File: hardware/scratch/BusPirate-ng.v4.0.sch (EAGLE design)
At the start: 142 parts, among them CON1 CON-USB-F-MICRO-B, IC1 IC_UC_STM32F103RBTXX-LQFP64, IC10 74LVC1G07DBV, IC11 IC_BUFF_SN74LVC1T45DBV, IC12 74LVC1G07DBV, IC13 IC_BUFF_SN74LVC1T45DBV, IC14 74LVC1G07DBV, IC15 IC_BUFF_SN74LVC1T45DBV, IC16 74LVC1G07DBV, IC17 IC_BUFF_SN74LVC1T45DBV, IC2 IC_MEM_23LC1024, IC3 IC_MEM_23LC1024, IC4 IC_74AC573, IC5 IC_BL1551, IC6 IC_BL1551, IC7 74HCT4066PW, IC8 74LVC1G07DBV, IC9 IC_BUFF_SN74LVC1T45DBV, J1 CON_HEADER_1X04, J2 CON_HEADER_1X03-PTH, J3 CON_HEADER_2X02-PTH, J4 CON_HEADER_1X10-RIGHT_ANGLED_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, U1 IC_FPGA_ICE40HX4K, U2 IC_UC_STM32F103ZX, U3 IC_MEM_AT45DB041D

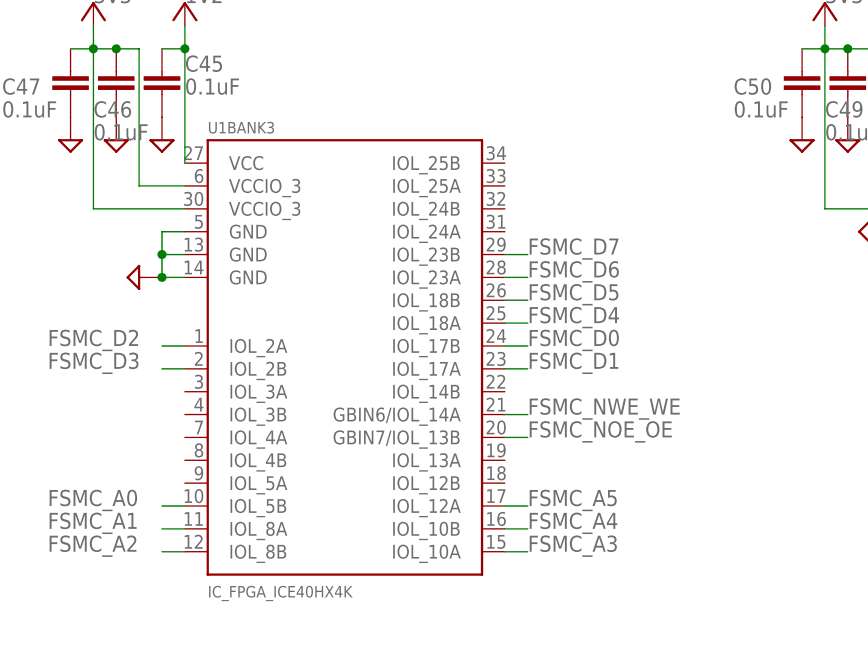
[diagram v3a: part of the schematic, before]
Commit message: removed connection FSMC_NOE_OE and FSMC_NEW_WE wired FSMC_D8 - FSMC_D15 to FPGA
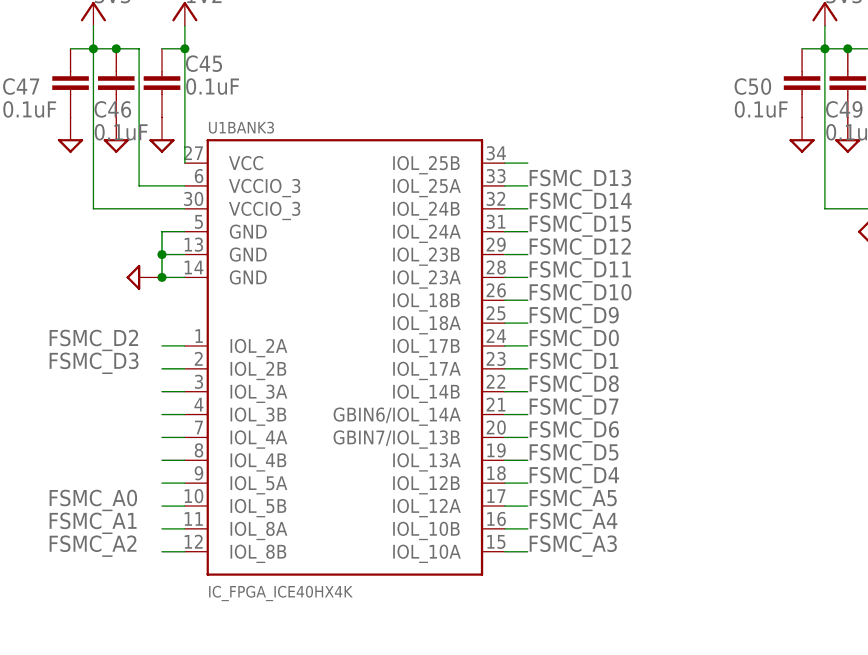
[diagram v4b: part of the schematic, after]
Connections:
- new net N$11: U1BANK3.IOL_3A
- new net N$15: U1BANK3.IOL_3B
- new net N$17: U1BANK3.IOL_25B
- new net N$19: U1BANK3.IOL_4A
- new net N$21: U1BANK3.IOL_4B
- new net N$22: U1BANK3.IOL_5A
- net FSMC_D10: now also U1BANK3.IOL_18B
- net FSMC_D11: now also U1BANK3.IOL_23A
- net FSMC_D12: now also U1BANK3.IOL_23B
- net FSMC_D13: now also U1BANK3.IOL_25A
- net FSMC_D14: now also U1BANK3.IOL_24B
- net FSMC_D15: now also U1BANK3.IOL_24A
- net FSMC_D4: now also U1BANK3.IOL_12B; no longer U1BANK3.IOL_18A
- net FSMC_D5: now also U1BANK3.IOL_13A; no longer U1BANK3.IOL_18B
- net FSMC_D6: now also U1BANK3.GBIN7/IOL_13B; no longer U1BANK3.IOL_23A
- net FSMC_D7: now also U1BANK3.GBIN6/IOL_14A; no longer U1BANK3.IOL_23B
- net FSMC_D8: now also U1BANK3.IOL_14B
- net FSMC_D9: now also U1BANK3.IOL_18A
- net FSMC_NOE_OE: no longer U1BANK3.GBIN7/IOL_13B
- net FSMC_NWE_WE: no longer U1BANK3.GBIN6/IOL_14A
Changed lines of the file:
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@@
 <label x="-241.3" y="416.56" size="1.778" layer="95"/>
+</segment>
+</net>
+<net name="FSMC_NWE_WE" class="0">
+<segment>
+<pinref part="U2" gate="U" pin="PD5/FT/FSMC_NWE/USART2_TX('1')"/>
+<wire x1="-215.9" y1="414.02" x2="-228.6" y2="414.02" width="0.1524" layer="91"/>
+<label x="-241.3" y="414.02" size="1.778" layer="95"/>
+</segment>
+</net>
+<net name="FSMC_D0" class="0">
+<segment>
+<pinref part="U2" gate="U" pin="PD14/FT/FSMC_D0/TIM4_CH3('1')"/>
+<wire x1="-215.9" y1="391.16" x2="-228.6" y2="391.16" width="0.1524" layer="91"/>
+<label x="-238.76" y="391.16" size="1.778" layer="95"/>
+</segment>
+<segment>
+<pinref part="U1" gate="BANK3" pin="IOL_17B"/>
+<wire x1="-2.54" y1="370.84" x2="0" y2="370.84" width="0.1524" layer="91"/>
+<label x="0" y="370.84" size="1.778" layer="95"/>
+</segment>
+</net>
+<net name="FSMC_D1" class="0">
+<segment>
+<pinref part="U2" gate="U" pin="PD15/FT/FSMC_D1/TIM4_CH4('1')"/>
+<wire x1="-215.9" y1="388.62" x2="-228.6" y2="388.62" width="0.1524" layer="91"/>
+<label x="-238.76" y="388.62" size="1.778" layer="95"/>
+</segment>
+<segment>
+<pinref part="U1" gate="BANK3" pin="IOL_17A"/>
+<wire x1="-2.54" y1="368.3" x2="0" y2="368.3" width="0.1524" layer="91"/>
+<label x="0" y="368.3" size="1.778" layer="95"/>
+</segment>
+</net>
+<net name="FSMC_D4" class="0">
+<segment>
+<pinref part="U2" gate="U" pin="PE7/FT/FSMC_D4/TIM1_ETR('11')"/>
+<wire x1="-215.9" y1="365.76" x2="-228.6" y2="365.76" width="0.1524" layer="91"/>
+<label x="-238.76" y="365.76" size="1.778" layer="95"/>
+</segment>
+<segment>
+<pinref part="U1" gate="BANK3" pin="IOL_12B"/>
+<wire x1="-2.54" y1="355.6" x2="0" y2="355.6" width="0.1524" layer="91"/>
+<label x="0" y="355.6" size="1.778" layer="95"/>
+</segment>
+</net>
+<net name="FSMC_D5" class="0">
+<segment>
+<pinref part="U2" gate="U" pin="PE8/FT/FSMC_D5/TIM1_CH1N('11')"/>
+<wire x1="-215.9" y1="363.22" x2="-228.6" y2="363.22" width="0.1524" layer="91"/>
+<label x="-238.76" y="363.22" size="1.778" layer="95"/>
+</segment>
+<segment>
+<pinref part="U1" gate="BANK3" pin="IOL_13A"/>
+<wire x1="-2.54" y1="358.14" x2="0" y2="358.14" width="0.1524" layer="91"/>
+<label x="0" y="358.14" size="1.778" layer="95"/>
+</segment>
+</net>
+<net name="FSMC_D6" class="0">
+<segment>
+<pinref part="U2" gate="U" pin="PE9/FT/FSMC_D6/TIM1_CH1('11')"/>
+<wire x1="-215.9" y1="360.68" x2="-228.6" y2="360.68" width="0.1524" layer="91"/>
+<label x="-238.76" y="360.68" size="1.778" layer="95"/>
 </segment>
 <segment>
@@
 </segment>
 </net>
-<net name="FSMC_NWE_WE" class="0">
-<segment>
-<pinref part="U2" gate="U" pin="PD5/FT/FSMC_NWE/USART2_TX('1')"/>
-<wire x1="-215.9" y1="414.02" x2="-228.6" y2="414.02" width="0.1524" layer="91"/>
-<label x="-241.3" y="414.02" size="1.778" layer="95"/>
+<net name="FSMC_D7" class="0">
+<segment>
+<pinref part="U2" gate="U" pin="PE10/FT/FSMC_D7/TIM1_CH2N('11')"/>
+<wire x1="-215.9" y1="358.14" x2="-228.6" y2="358.14" width="0.1524" layer="91"/>
+<label x="-238.76" y="358.14" size="1.778" layer="95"/>
 </segment>
 <segment>
@@
 <wire x1="-2.54" y1="363.22" x2="0" y2="363.22" width="0.1524" layer="91"/>
 <label x="0" y="363.22" size="1.778" layer="95"/>
-</segment>
-</net>
-<net name="FSMC_D0" class="0">
-<segment>
-<pinref part="U2" gate="U" pin="PD14/FT/FSMC_D0/TIM4_CH3('1')"/>
-<wire x1="-215.9" y1="391.16" x2="-228.6" y2="391.16" width="0.1524" layer="91"/>
-<label x="-238.76" y="391.16" size="1.778" layer="95"/>
-</segment>
-<segment>
-<pinref part="U1" gate="BANK3" pin="IOL_17B"/>
-<wire x1="-2.54" y1="370.84" x2="0" y2="370.84" width="0.1524" layer="91"/>
-<label x="0" y="370.84" size="1.778" layer="95"/>
-</segment>
-</net>
-<net name="FSMC_D1" class="0">
-<segment>
-<pinref part="U2" gate="U" pin="PD15/FT/FSMC_D1/TIM4_CH4('1')"/>
-<wire x1="-215.9" y1="388.62" x2="-228.6" y2="388.62" width="0.1524" layer="91"/>
-<label x="-238.76" y="388.62" size="1.778" layer="95"/>
-</segment>
-<segment>
-<pinref part="U1" gate="BANK3" pin="IOL_17A"/>
-<wire x1="-2.54" y1="368.3" x2="0" y2="368.3" width="0.1524" layer="91"/>
-<label x="0" y="368.3" size="1.778" layer="95"/>
-</segment>
-</net>
-<net name="FSMC_D4" class="0">
-<segment>
-<pinref part="U2" gate="U" pin="PE7/FT/FSMC_D4/TIM1_ETR('11')"/>
-<wire x1="-215.9" y1="365.76" x2="-228.6" y2="365.76" width="0.1524" layer="91"/>
-<label x="-238.76" y="365.76" size="1.778" layer="95"/>
-</segment>
-<segment>
-<pinref part="U1" gate="BANK3" pin="IOL_18A"/>
-<wire x1="-2.54" y1="373.38" x2="0" y2="373.38" width="0.1524" layer="91"/>
-<label x="0" y="373.38" size="1.778" layer="95"/>
-</segment>
-</net>
-<net name="FSMC_D5" class="0">
-<segment>
-<pinref part="U2" gate="U" pin="PE8/FT/FSMC_D5/TIM1_CH1N('11')"/>
-<wire x1="-215.9" y1="363.22" x2="-228.6" y2="363.22" width="0.1524" layer="91"/>
-<label x="-238.76" y="363.22" size="1.778" layer="95"/>
-</segment>
-<segment>
-<pinref part="U1" gate="BANK3" pin="IOL_18B"/>
-<wire x1="-2.54" y1="375.92" x2="0" y2="375.92" width="0.1524" layer="91"/>
-<label x="0" y="375.92" size="1.778" layer="95"/>
-</segment>
-</net>
-<net name="FSMC_D6" class="0">
-<segment>
-<pinref part="U2" gate="U" pin="PE9/FT/FSMC_D6/TIM1_CH1('11')"/>
-<wire x1="-215.9" y1="360.68" x2="-228.6" y2="360.68" width="0.1524" layer="91"/>
-<label x="-238.76" y="360.68" size="1.778" layer="95"/>
-</segment>
-<segment>
-<pinref part="U1" gate="BANK3" pin="IOL_23A"/>
-<wire x1="-2.54" y1="378.46" x2="0" y2="378.46" width="0.1524" layer="91"/>
-<label x="0" y="378.46" size="1.778" layer="95"/>
-</segment>
-</net>
-<net name="FSMC_D7" class="0">
-<segment>
-<pinref part="U2" gate="U" pin="PE10/FT/FSMC_D7/TIM1_CH2N('11')"/>
-<wire x1="-215.9" y1="358.14" x2="-228.6" y2="358.14" width="0.1524" layer="91"/>
-<label x="-238.76" y="358.14" size="1.778" layer="95"/>
-</segment>
-<segment>
-<pinref part="U1" gate="BANK3" pin="IOL_23B"/>
-<wire x1="-2.54" y1="381" x2="0" y2="381" width="0.1524" layer="91"/>
-<label x="0" y="381" size="1.778" layer="95"/>
 </segment>
 </net>
@@
 <label x="-238.76" y="355.6" size="1.778" layer="95"/>
 </segment>
+<segment>
+<pinref part="U1" gate="BANK3" pin="IOL_14B"/>
+<wire x1="-2.54" y1="365.76" x2="0" y2="365.76" width="0.1524" layer="91"/>
+<label x="0" y="365.76" size="1.778" layer="95"/>
+</segment>
 </net>
 <net name="FSMC_D9" class="0">
@@
 <label x="-238.76" y="353.06" size="1.778" layer="95"/>
 </segment>
+<segment>
+<pinref part="U1" gate="BANK3" pin="IOL_18A"/>
+<wire x1="-2.54" y1="373.38" x2="0" y2="373.38" width="0.1524" layer="91"/>
+<label x="0" y="373.38" size="1.778" layer="95"/>
+</segment>
 </net>
 <net name="FSMC_D10" class="0">
@@
 <label x="-238.76" y="350.52" size="1.778" layer="95"/>
 </segment>
+<segment>
+<pinref part="U1" gate="BANK3" pin="IOL_18B"/>
+<wire x1="-2.54" y1="375.92" x2="0" y2="375.92" width="0.1524" layer="91"/>
+<label x="0" y="375.92" size="1.778" layer="95"/>
+</segment>
 </net>
 <net name="FSMC_D11" class="0">
@@
 <label x="-238.76" y="347.98" size="1.778" layer="95"/>
 </segment>
+<segment>
+<pinref part="U1" gate="BANK3" pin="IOL_23A"/>
+<wire x1="-2.54" y1="378.46" x2="0" y2="378.46" width="0.1524" layer="91"/>
+<label x="0" y="378.46" size="1.778" layer="95"/>
+</segment>
 </net>
 <net name="FSMC_D12" class="0">
@@
 <label x="-238.76" y="345.44" size="1.778" layer="95"/>
 </segment>
+<segment>
+<pinref part="U1" gate="BANK3" pin="IOL_23B"/>
+<wire x1="-2.54" y1="381" x2="0" y2="381" width="0.1524" layer="91"/>
+<label x="0" y="381" size="1.778" layer="95"/>
+</segment>
 </net>
 <net name="FSMC_D13" class="0">
@@
 <label x="-241.3" y="406.4" size="1.778" layer="95"/>
 </segment>
+<segment>
+<pinref part="U1" gate="BANK3" pin="IOL_25A"/>
+<wire x1="-2.54" y1="388.62" x2="0" y2="388.62" width="0.1524" layer="91"/>
+<label x="0" y="388.62" size="1.778" layer="95"/>
+</segment>
 </net>
 <net name="FSMC_D14" class="0">
@@
 <label x="-241.3" y="403.86" size="1.778" layer="95"/>
 </segment>
+<segment>
+<pinref part="U1" gate="BANK3" pin="IOL_24B"/>
+<wire x1="-2.54" y1="386.08" x2="0" y2="386.08" width="0.1524" layer="91"/>
+<label x="0" y="386.08" size="1.778" layer="95"/>
+</segment>
 </net>
 <net name="FSMC_D15" class="0">
@@
 <label x="-241.3" y="401.32" size="1.778" layer="95"/>
 </segment>
-</net>
+<segment>
+<pinref part="U1" gate="BANK3" pin="IOL_24A"/>
+<wire x1="-2.54" y1="383.54" x2="0" y2="383.54" width="0.1524" layer="91"/>
+<label x="0" y="383.54" size="1.778" layer="95"/>
+</segment>
+</net>
+<net name="N$17" class="0">
+<segment>
+<pinref part="U1" gate="BANK3" pin="IOL_25B"/>
+<wire x1="-2.54" y1="391.16" x2="0" y2="391.16" width="0.1524" layer="91"/>
+</segment>
+</net>
+<net name="N$11" class="0">
+<segment>
+<pinref part="U1" gate="BANK3" pin="IOL_3A"/>
+<wire x1="-38.1" y1="365.76" x2="-40.64" y2="365.76" width="0.1524" layer="91"/>
+</segment>
+</net>
+<net name="N$15" class="0">
+<segment>
+<pinref part="U1" gate="BANK3" pin="IOL_3B"/>
+<wire x1="-38.1" y1="363.22" x2="-40.64" y2="363.22" width="0.1524" layer="91"/>
+</segment>
+</net>
+<net name="N$19" class="0">
+<segment>
+<pinref part="U1" gate="BANK3" pin="IOL_4A"/>
+<wire x1="-38.1" y1="360.68" x2="-40.64" y2="360.68" width="0.1524" layer="91"/>
+</segment>
+</net>
+<net name="N$21" class="0">
+<segment>
+<pinref part="U1" gate="BANK3" pin="IOL_4B"/>
+<wire x1="-38.1" y1="358.14" x2="-40.64" y2="358.14" width="0.1524" layer="91"/>
+</segment>
+</net>
+<net name="N$22" class="0">
+<segment>
+<pinref part="U1" gate="BANK3" pin="IOL_5A"/>
+<wire x1="-38.1" y1="355.6" x2="-40.64" y2="355.6" width="0.1524" layer="91"/>
+</segment>
+</net>

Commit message: wired: -IO headers -CRESET -CDONE -MCU_MCO (Master Clock Out) to FPGA -FPGA to IO buffers -VCCPLL with 0.1uF cap and GNDPLL -2 interrupts from FPGA but not yet connected
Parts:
- added C55: 0.1uF, rcl:C-EUC0603
- added J5: CON_HEADER_1X10-RIGHT_ANGLED_PTH_SHROUDED, dp_devices.v6:CON_HEADER_1X10-RIGHT_ANGLED_PTH_SHROUDED
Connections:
- removed net N$11: U1BANK3.IOL_3A
- removed net N$12: R38.1, U1BANK2.CRESET_B
- removed net N$14: R39.1, U1BANK2.CDONE
- new net FPGA_CDONE: R39.1, U1BANK2.CDONE, U2U.I2C2_SDA/USART3_RX('00')/TIM2_CH4('10'OR'11')/FT/PB11
- new net FPGA_CRESET: R38.1, U1BANK2.CRESET_B, U2U.I2C2_SCL/USART3_TX('00')/TIM2_CH3('10'OR'11')/FT/PB10
- new net MCU_INT0: U1BANK2.GBIN4/IOB_82
- new net MCU_INT1: U1BANK2.GBIN5/IOB_81
- new net MCU_MCO: U1BANK3.GBIN7/IOL_13B, U2U.PA8/FT/USART1_CK/TIM1_CH1('00'OR'01')/MCO
- new net N$10: U2U.PG0/FT/FSMC_A10
- new net N$23: U1BANK0.IOT_168
- new net N$24: U1BANK0.GBIN0/IOT_198
- new net N$25: U1BANK0.GBIN1/IOT_197
- net 1V2: now also C55.2, U1BANK2.VCCPLL0
- net BPIO_AUX: now also J5.6
- net BPIO_CLOCK: now also J5.9
- net BPIO_CS: now also J5.7
- net BPIO_MISO: now also J5.8
- net BPIO_MOSI: now also J5.10
- net BUFDIR_AUX: now also U1BANK1.IOR_144
- net BUFDIR_CLOCK: now also U1BANK1.IOR_164
- net BUFDIR_CS: now also U1BANK1.IOR_139
- net BUFDIR_MISO: now also U1BANK1.IOR_152
- net BUFDIR_MOSI: now also U1BANK1.IOR_167
- net BUFIO_AUX: now also U1BANK1.GBIN2/IOR_141
- net BUFIO_CLOCK: now also U1BANK1.IOR_161
- net BUFIO_CS: now also U1BANK1.IOR_138
- net BUFIO_MISO: now also U1BANK1.IOR_148
- net BUFIO_MOSI: now also U1BANK1.IOR_166
- net BUFOD_AUX: now also U1BANK1.GBIN3/IOR_140
- net BUFOD_CLOCK: now also U1BANK1.IOR_160
- net BUFOD_CS: now also U1BANK1.IOR_137
- net BUFOD_MISO: now also U1BANK1.IOR_147
- net BUFOD_MOSI: now also U1BANK1.IOR_165
- net FSMC_A0: now also U1BANK3.IOL_3A; no longer U1BANK3.IOL_5B
- net FSMC_A1: now also U1BANK3.IOL_3B; no longer U1BANK3.IOL_8A
- net FSMC_A2: now also U1BANK3.IOL_4A; no longer U1BANK3.IOL_8B
- net FSMC_A3: now also U1BANK3.IOL_4B; no longer U1BANK3.IOL_10A
- net FSMC_A4: now also U1BANK3.IOL_5A; no longer U1BANK3.IOL_10B
- net FSMC_A5: now also U1BANK3.IOL_5B; no longer U1BANK3.IOL_12A
- net FSMC_D4: now also U1BANK3.IOL_10A; no longer U1BANK3.IOL_12B
- net FSMC_D5: now also U1BANK3.IOL_10B; no longer U1BANK3.IOL_13A
- net FSMC_D6: now also U1BANK3.IOL_12A; no longer U1BANK3.GBIN7/IOL_13B
- net FSMC_D7: now also U1BANK3.IOL_12B; no longer U1BANK3.GBIN6/IOL_14A
- net FSMC_D8: now also U1BANK3.IOL_13A; no longer U1BANK3.IOL_14B
- net GND: now also C55.1, J5.1, U1BANK0.GNDPLL1, U1BANK2.GNDPLL0
- net IO_ADC/DAC: now also J5.5
- net N$15: now also U1BANK3.IOL_8A; no longer U1BANK3.IOL_3B
- net N$19: now also U1BANK3.IOL_8B; no longer U1BANK3.IOL_4A
- net N$21: now also U1BANK3.GBIN6/IOL_14A; no longer U1BANK3.IOL_4B
- net N$22: now also U1BANK3.IOL_14B; no longer U1BANK3.IOL_5A
- net SWV33: now also J5.3
- net SWV50: now also J5.2
- net VEXTERN: now also J5.4
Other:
- note removed: "gndpll nc?!?"

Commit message: wired Logic analyzer circuit to FPGA
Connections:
- net IO_OE: now also U1BANK0.IOT_206
- net LA_AUX0: now also U1BANK0.IOT_215
- net LA_CLK: now also U1BANK0.IOT_221
- net LA_CS: now also U1BANK0.IOT_219
- net LA_HOLD: now also U1BANK0.IOT_212
- net LA_MISO: now also U1BANK0.IOT_222
- net LA_MOSI: now also U1BANK0.IOT_220
- net LA_SWV33: now also U1BANK0.IOT_214
- net LA_SWV50: now also U1BANK0.IOT_213
- net SRAM_CLK: now also U1BANK0.IOT_217
- net SRAM_CS: now also U1BANK0.IOT_216
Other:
- moved on the sheet: C14, C15, C17, IC2, IC3, IC4

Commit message: routing started, switch to bigger DP8556 PCB
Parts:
- removed C1, C3: 22pF, rcl:C-EUC0603
- removed C10, C2, C20, C4, C5, C7, C8, C9: 0.1uF, rcl:C-EUC0603
- removed C6: 1uF, rcl:CPOL-EUSMCA
- removed IC1: IC_UC_STM32F103RBTXX-LQFP64, dp_devices:IC_UC_STM32F103RBTXX-LQFP64
- removed PCB1: PCB_DP_RECTANGLE-80X49, dp_devices:PCB_DP_RECTANGLE-80X49
- removed R1: 10K, dp_devices:RESISTOR-0603
- removed XTAL1: 8Mhz, dp_devices:OSC-XTAL-12M
- added PCB2: PCB_DP_RECTANGLE-85X56, dp_blank_pcb:PCB_DP_RECTANGLE-85X56
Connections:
- removed net N$16: C3.2, IC1.PD0/5V/OSC_IN, XTAL1.2
- removed net N$20: C1.2, IC1.PD1/5V/OSC_OUT, XTAL1.1
- net 3V3: no longer C10.2, C20.2, C4.2, C5.2, C6.+, C7.2, C8.2, C9.2, IC1.VBAT, IC1.VDDA, IC1.VDD_1, IC1.VDD_2, IC1.VDD_3, IC1.VDD_4
- net ADC1: no longer IC1.TIM3_CH4/ADC9/PB1
- net ADC2: no longer IC1.ADC13/PC3
- net ADC3: no longer IC1.ADC11/PC1
- net ADC4: no longer IC1.ADC12/PC2
- net ADC5: no longer IC1.ADC10/PC0
- net ADC6: no longer IC1.ADC14/PC4
- net AUX0: no longer IC1.PD2/5V/TIM3_ETR, IC1.TIM3_CH3/ADC8/PB0
- net BOOT0: no longer IC1.BOOT0
- net BOOT1: no longer IC1.BOOT1/5V/PB2
- net CLOCK: no longer IC1.I2C1_SCL/TIM4_CH1/5V/PB6, IC1.SPI2_SCK/USART3_CTS/TIM1_CH1N/5V/PB13
- net CS: no longer IC1.SPI2_NSS/I2C2_SMBAI/USART3_CK/TIM1_BKIN/5V/PB12
- net GND: no longer C1.1, C10.1, C2.1, C20.1, C3.1, C4.1, C5.1, C6.-, C7.1, C8.1, C9.1, IC1.VSSA, IC1.VSS_1, IC1.VSS_2, IC1.VSS_3, IC1.VSS_4, R1.2
- net IO_OE: no longer IC1.5V/PC7
- net LA_AUX0: no longer IC1.PA4/ADC4/USART2_CK/SPI1_NSS
- net LA_CLK: no longer IC1.PA1/ADC1/USART2_RTS/TIM2_CH2
- net LA_CS: no longer IC1.PA3/ADC3/USART2_RX/TIM2_CH4
- net LA_HOLD: no longer IC1.PA7/ADC7/SPI1_MOSI/TIM3_CH2
- net LA_MISO: no longer IC1.PA2/ADC2/USART2_TX/TIM2_CH4
- net LA_MOSI: no longer IC1.PA0/ADC0/USART2_CTS/TIM2_CH1_ETR/WKUP
- net LA_SWV33: no longer IC1.PA5/ADC5/SPI1_SCK
- net LA_SWV50: no longer IC1.PA6/ADC6/SPI1_MISO/TIM3_CH1
- net LD1: no longer IC1.5V/PC8
- net MISO: no longer IC1.I2C2_SDA/USART3_RX/5V/PB11, IC1.SPI2_MISO/USART3_RTS/TIM1_CH2N/5V/PB14
- net MOSI: no longer IC1.I2C1_SDA/TIM4_CH2/5V/PB7, IC1.I2C2_SCL/USART3_TX/5V/PB10, IC1.SPI2_MOSI/TIM1_CH3N/5V/PB15
- net MS0: no longer IC1.TIM4_CH3/5V/PB8
- net RST: no longer C2.2, IC1.NRST
- net SRAM_CLK: no longer IC1.PA8/5V/USART1_CK/TIM1_CH1/MCO
- net SRAM_CS: no longer IC1.JTDO/5V/PB3
- net SWCLK: no longer IC1.PA14/5V/JTCK/SWCLK
- net SWDIO: no longer IC1.PA13/5V/JTMS/SWDIO
- net UART_RX: no longer IC1.PA10/5V/USART1_RX/TIM1_CH3
- net UART_TX: no longer IC1.PA9/5V/USART1_TX/TIM1_CH2
- net USBLED: no longer IC1.5V/PC9
- net USB_D+: no longer IC1.PA12/5V/USART1_RTS/TIM1_ETR/CAN_TX/USB_D+
- net USB_D-: no longer IC1.PA11/5V/USART1_CTS/TIM1_CH4/CAN_RX/USB_D-
- net USB_DET: no longer IC1.PA15/5V/JTDI
- net V33PU: no longer IC1.I2C1_SMBAI/PB5
- net V50PU: no longer IC1.JNTRST/5V/PB4
- net VEXTPU: no longer IC1.5V/PC6
- net VREGEN: no longer IC1.TIM4_CH4/5V/PB9, R1.1
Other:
- note removed: "STM32F103"
- note removed: "wire SRAM_CLK to FPGA global pin clock"
- moved on the sheet: C36, C37, C51, C52, C53, C54, R40, U2, XTAL2

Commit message: individualy wired SRAM to FPGA and LATCH to FPGA, continue routing
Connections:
- removed net LA_AUX0: IC3IC.SI/SIO0, IC4IC.4Q, U1BANK0.IOT_215
- removed net LA_CLK: IC2IC.SO/SIO1, IC4IC.7Q, U1BANK0.IOT_221
- removed net LA_CS: IC2IC.!HOLD/SIO3, IC4IC.5Q, U1BANK0.IOT_219
- removed net LA_HOLD: IC3IC.!HOLD/SIO3, U1BANK0.IOT_212
- removed net LA_MISO: IC2IC.SI/SIO0, IC4IC.6Q, U1BANK0.IOT_222
- removed net LA_MOSI: IC2IC.SIO2, IC4IC.8Q, U1BANK0.IOT_220
- removed net LA_SWV33: IC3IC.SO/SIO1, IC4IC.3Q, U1BANK0.IOT_214
- removed net LA_SWV50: IC3IC.SIO2, IC4IC.2Q, U1BANK0.IOT_213
- new net LA_LAT_AUX0: IC4IC.4Q, U1BANK0.IOT_170
- new net LA_LAT_CLK: IC4IC.7Q, U1BANK0.IOT_173
- new net LA_LAT_CS: IC4IC.5Q, U1BANK0.IOT_171
- new net LA_LAT_MISO: IC4IC.6Q, U1BANK0.IOT_172
- new net LA_LAT_MOSI: IC4IC.8Q, U1BANK0.IOT_174
- new net LA_LAT_SWV33: IC4IC.3Q, U1BANK0.IOT_169
- new net LA_LAT_SWV50: IC4IC.2Q, U1BANK0.IOT_168
- new net LA_MEM_AUX0: IC3IC.SI/SIO0, U1BANK0.IOT_212
- new net LA_MEM_CLK: IC2IC.SO/SIO1, U1BANK0.IOT_220
- new net LA_MEM_CS: IC2IC.!HOLD/SIO3, U1BANK0.IOT_221
- new net LA_MEM_HOLD: IC3IC.!HOLD/SIO3, U1BANK0.IOT_215
- new net LA_MEM_MISO: IC2IC.SI/SIO0, U1BANK0.IOT_216
- new net LA_MEM_MOSI: IC2IC.SIO2, U1BANK0.IOT_217
- new net LA_MEM_SWV33: IC3IC.SO/SIO1, U1BANK0.IOT_214
- new net LA_MEM_SWV50: IC3IC.SIO2, U1BANK0.IOT_213
- new net N$11: U1BANK0.IOT_192
- new net N$12: U1BANK0.IOT_191
- new net N$14: U1BANK0.IOT_190
- new net N$16: U1BANK0.IOT_181
- new net N$20: U1BANK0.IOT_179
- new net N$26: U1BANK0.IOT_178
- new net N$27: U2U.PE2/FT/FSMC_A23
- net N$23: now also U1BANK0.IOT_177; no longer U1BANK0.IOT_168
- net SRAM_CLK: now also U1BANK0.IOT_219; no longer U1BANK0.IOT_217
- net SRAM_CS: now also U1BANK0.IOT_222; no longer U1BANK0.IOT_216
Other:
- note added: "FPGA Unconnected"
